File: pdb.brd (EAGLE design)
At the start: 50 x 100 mm, 40 parts, among them Q1 20MHz, Q2 IRFR5305PBF, Q3 IRFR5305PBF, U1 TSR_1-2433, U2 LTC2946CMSPBF, U3 LTC2946CMSPBF, U4 LTC2946CMSPBF, U5 ATMEGA48-20AU, U6 TXB0104, U7 AT30TS74SS8M

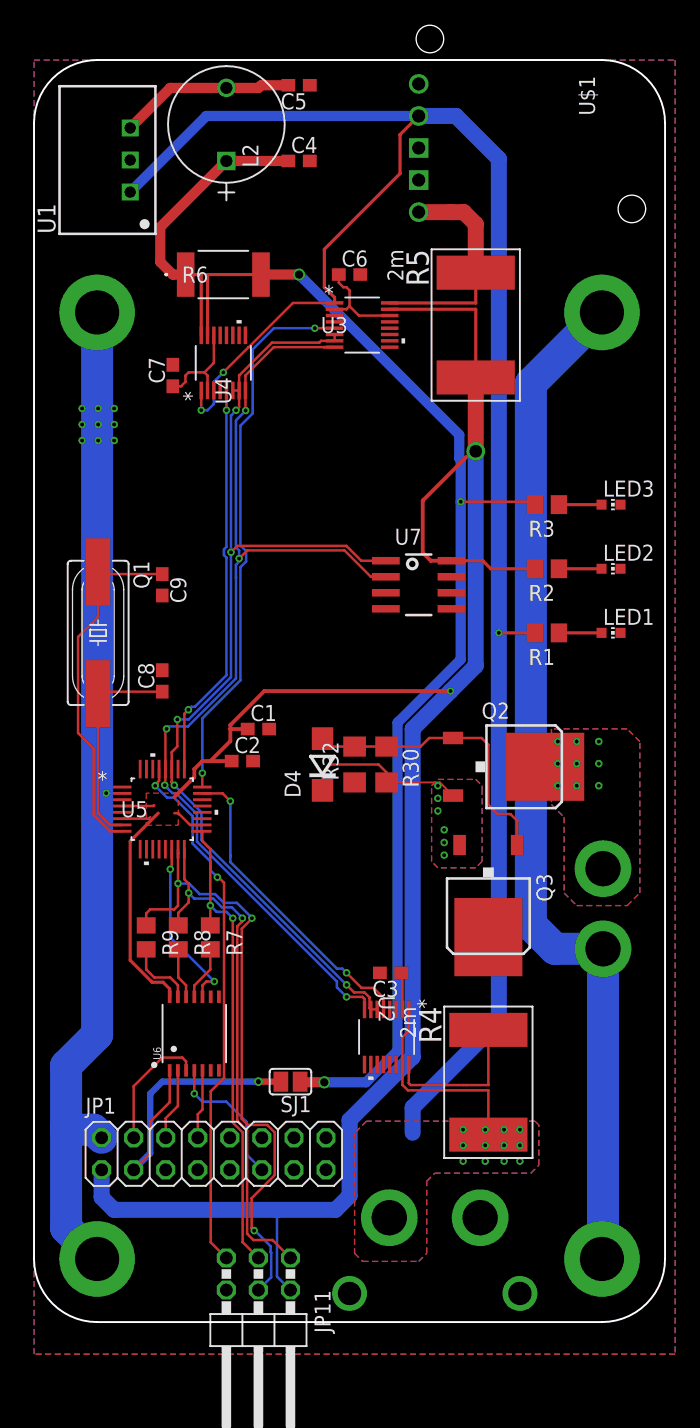
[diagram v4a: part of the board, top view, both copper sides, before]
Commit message: multiple changes
removed inductor,
fixed layout + schematic
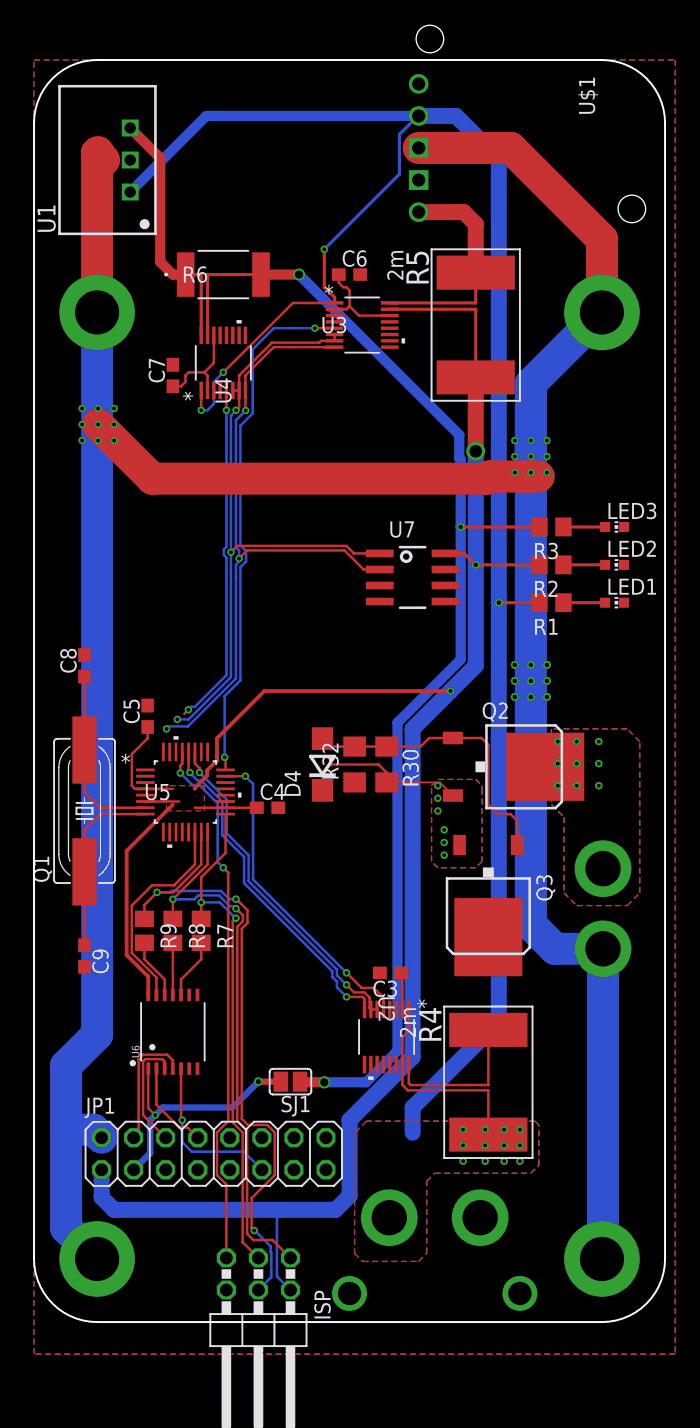
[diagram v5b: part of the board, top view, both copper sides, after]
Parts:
- removed C1, C2: 100nF, rcl:C0603
- removed L2: RLB9012-221KL, jonas_bourns:IND_BOURNS_RLB9012
- C4, C5: device resistor:C0603 -> rcl:C0603
- moved C5 51.4 mm to (9.00, 48.0), turned to 90 degrees
- moved C4 51.3 mm to (18.5, 40.8)
- moved C9 30.1 mm to (4.00, 29.0)
- moved Q1 14.2 mm to (4.00, 40.5), turned to 90 degrees
- moved C8 6.28 mm to (4.00, 52.0)
- moved R1 2.42 mm to (41.0, 57.0)
- moved LED1 2.41 mm to (46.0, 57.0)
- moved U5 2.29 mm to (12.0, 42.0)
- moved R3 1.81 mm to (41.0, 63.0)
- moved LED3 1.79 mm to (46.0, 63.0)
- moved U6 1.71 mm to (11.0, 23.0)
- moved R7 0.89 mm to (13.2, 31.0)
- moved U7 0.75 mm to (30.0, 59.0)
- moved R8 0.67 mm to (11.0, 31.0)
- moved R9 0.54 mm to (8.75, 31.0)
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- renumbered JP11 to ISP
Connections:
- removed net N$6: C5.2, L2.2, U1.3
- removed net N$8: R7.2, U6.11
- new net N$3: R7.2, U6.10
- net +5V: now also C4.1, C5.1; no longer C1.1, C2.1
- net EXT_SPI_CLK: now also U6.5; no longer U6.4
- net EXT_SPI_CS: now also U6.2; no longer U6.5
- net EXT_SPI_MISO: now also U6.4; no longer U6.3
- net EXT_SPI_MOSI: now also U6.3; no longer U6.2
- net GND: now also C5.2; no longer C1.2, C2.2, C5.1
- net N$1: now also R8.2, U6.11; no longer R9.2, U6.13
- net N$2: now also R9.2; no longer R8.2
- net SENSE+3V3: now also U1.3; no longer C4.1, L2.1
- net SS_5V: now also U6.13; no longer U6.10
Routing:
- net GND: track 162.1 -> 240.8 mm, vias 15 -> 32
- net N$6: track 13.9 -> 0.00 mm
- net N$28: track 28.4 -> 14.5 mm
- net +5V: track 183.4 -> 176.7 mm, vias 2 -> 3
- net EXT_3V3: track 26.4 -> 20.0 mm, vias 1 -> 2
- net N$3: track 0.00 -> 4.79 mm
- net !ALERT_3V3: track 31.7 -> 27.3 mm
- net N$8: track 4.28 -> 0.00 mm
- net SDA: track 83.4 -> 79.2 mm
- net EXT_SPI_MOSI: track 5.74 -> 9.35 mm
- net SENSE+3V3: track 23.6 -> 20.1 mm
- net SCL: track 82.2 -> 78.9 mm
- net SS_5V: track 13.9 -> 16.8 mm, vias 2 -> 0
- net MISO_5V: track 41.5 -> 44.3 mm
- net MOSI_5V: track 48.9 -> 51.5 mm
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
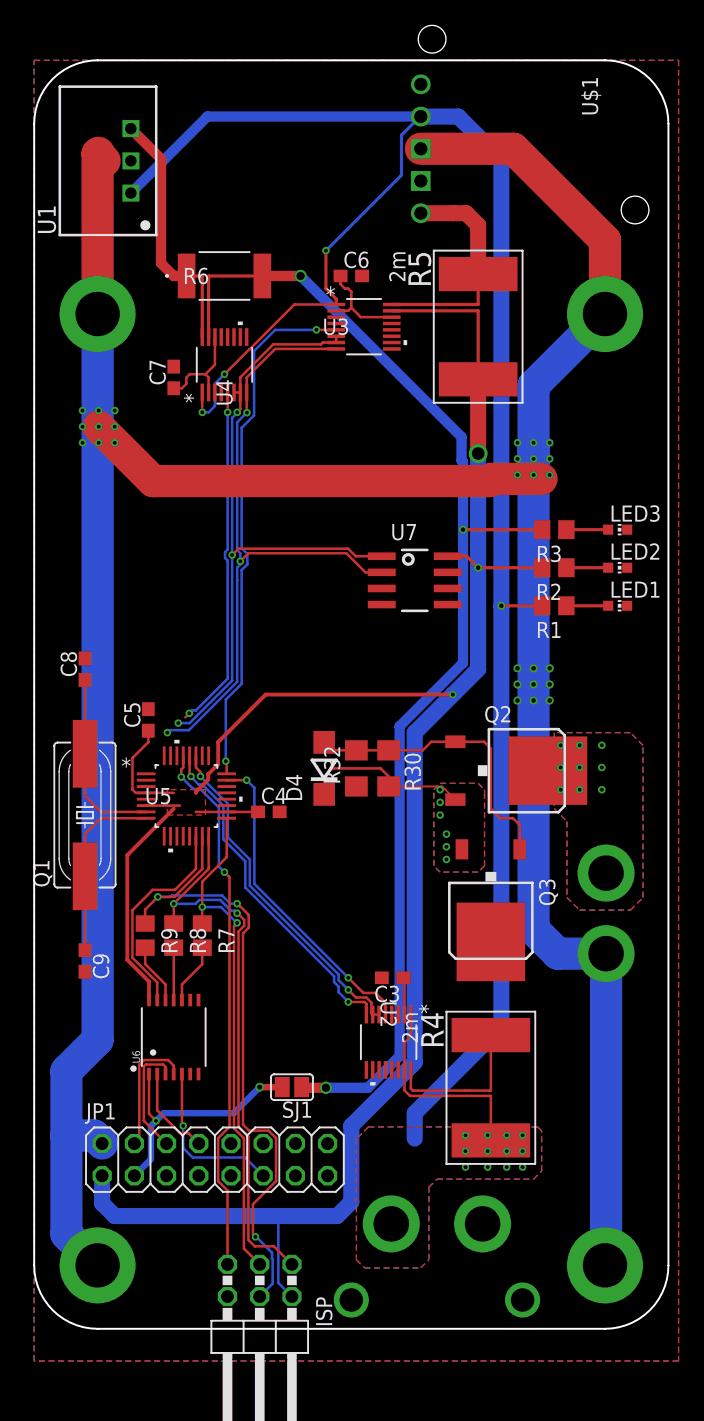
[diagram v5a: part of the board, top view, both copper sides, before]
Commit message: various changes
moved smd components on metric grid
silkscreen, reduced fuckup in part sizes
added output
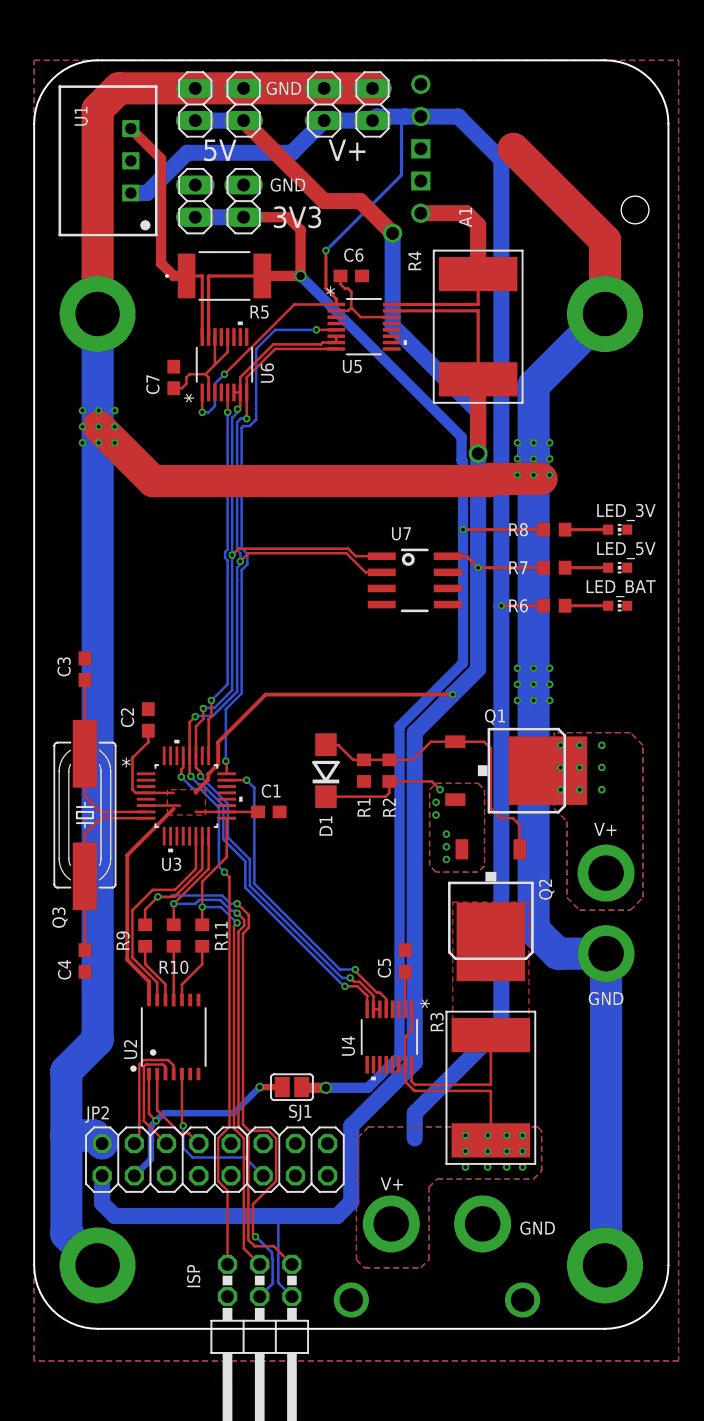
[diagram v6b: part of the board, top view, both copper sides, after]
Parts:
- removed C8, C9: 22pF, rcl:C0603
- removed D4: ZD18, diode:DO214BA
- removed R30: 10k, rcl:R1206
- removed R32: 1k, rcl:R1206
- removed U$1: D24V50F5, niklas_pololu:D24V50F5
- added A1: D24V50F5SINGLESCREW, jonas_pololu:D24V50F5_SINGLESCREW
- added C1, C2: 100nF, resistor:C0603
- added D1: ZD18, diode:DO214BA
- added JP2: (no value), pinhead:2X08
- added JP3, JP4, JP5, JP6, JP7: (no value), pinhead:1X02
- added R10, R11: 4,7k, resistor:R0603
- C3: value 0,1µF -> 22pF; device rcl:C0603 -> resistor:C0603
- C4: value 100nF -> 22pF; device rcl:C0603 -> resistor:C0603
- C5: value 100nF -> 0,1µF; device rcl:C0603 -> resistor:C0603
- C6, C7: device rcl:C0603 -> resistor:C0603
- JP1: device pinhead:2X08 -> pinhead:1X02
- Q1: value 20MHz -> IRFR5305PBF; device crystal:HC49UP -> transistor-power:D-PAK_TO252AA
- Q3: value IRFR5305PBF -> 20MHz; device transistor-power:D-PAK_TO252AA -> crystal:HC49UP
- R1: value 1,2k -> 1k; device rcl:R0805 -> resistor:R0603
- R2: value 250 -> 10k; device rcl:R0805 -> resistor:R0603
- R3: value 100 -> 2m; device rcl:R0805 -> jonas_resistor:3920
- R5: value 2m -> CRA2512-FZ-R040ELF; device jonas_resistor:3920 -> jonas_bourns:BO_CRA2512
- R6: value CRA2512-FZ-R040ELF -> 1,2k; device jonas_bourns:BO_CRA2512 -> resistor:R0603
- R7: value 4,7k -> 250; device rcl:R0805 -> resistor:R0603
- R8: value 4,7k -> 100; device rcl:R0805 -> resistor:R0603
- R9: device rcl:R0805 -> resistor:R0603
- U2: value LTC2946CMSPBF -> TXB0104; device niklas_lt:MSOP-16_MS -> SparkFun-IC-Comms:TSSOP14
- U3: value LTC2946CMSPBF -> ATMEGA48-20AU; device niklas_lt:MSOP-16_MS -> niklas_atmel:32A
- U5: value ATMEGA48-20AU -> LTC2946CMSPBF; device niklas_atmel:32A -> niklas_lt:MSOP-16_MS
- U6: value TXB0104 -> LTC2946CMSPBF; device SparkFun-IC-Comms:TSSOP14 -> niklas_lt:MSOP-16_MS
- moved JP1 84.1 mm to (26.7, 96.5), turned to 90 degrees
- moved R4 60.0 mm to (35.0, 79.0)
- moved U4 54.6 mm to (28.0, 23.0), turned to 270 degrees
- moved U6 53.2 mm to (15.0, 76.0), turned to 90 degrees
- moved R3 44.3 mm to (36.0, 19.0), turned to 270 degrees
- moved R8 43.9 mm to (41.0, 63.0), turned to 180 degrees
- moved R7 40.1 mm to (41.0, 60.0), turned to 180 degrees
- moved U3 39.6 mm to (12.0, 42.0)
- moved U5 39.6 mm to (26.0, 79.0)
- moved R6 36.8 mm to (41.0, 57.0), turned to 180 degrees
- moved C3 34.4 mm to (4.00, 52.0), turned to 90 degrees
- moved Q1 34.2 mm to (38.0, 44.0), turned to 270 degrees
- moved Q3 32.9 mm to (4.00, 40.5), turned to 90 degrees
- moved C5 27.8 mm to (29.2, 29.0)
- moved R2 20.6 mm to (28.0, 44.0), turned to 270 degrees
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- renumbered ESC to J1, LED1 to LED_BAT, LED2 to LED_5V, LED3 to LED_3V
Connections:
- net !ALERT_3V3: now also U3.25, U6.5; no longer U4.5, U5.25
- net !ALERT_5V: now also U3.24, U5.5; no longer U3.5, U5.24
- net !ALERT_V+: now also U3.23, U4.5; no longer U2.5, U5.23
- net +3V3: now also JP6.1, JP7.1, R5.2, R8.2, U6.15; no longer R3.2, R6.2, U4.15
- net +5V: now also C1.1, C2.1, JP2.1, JP4.1, JP5.1, R4.P$2, R7.2, U2.14, U3.18, U3.4, U3.6, U5.15; no longer C4.1, C5.1, JP1.1, R2.2, R5.P$2, U3.15, U5.18, U5.4, U5.6, U6.14
- net AKKU-ZWISCHEN: now also D1.C, Q1.3, R2.2; no longer D4.C, Q3.3, R30.2
- net BAT_IN: now also Q1.4; no longer Q2.4
- net EXT_!RST: now also JP2.16; no longer JP1.16
- net EXT_3V3: now also JP2.3, U2.1; no longer JP1.3, U6.1
- net EXT_A0: now also JP2.9; no longer JP1.9
- net EXT_A3: now also JP2.7; no longer JP1.7
- net EXT_A4: now also JP2.5; no longer JP1.5
- net EXT_D1: now also JP2.14; no longer JP1.14
- net EXT_D2: now also JP2.12; no longer JP1.12
- net EXT_D9: now also JP2.10; no longer JP1.10
- net EXT_SCL_5V: now also JP2.13; no longer JP1.13
- net EXT_SDA_5V: now also JP2.15; no longer JP1.15
- net EXT_SPI_CLK: now also JP2.11, U2.5; no longer JP1.11, U6.5
- net EXT_SPI_CS: now also JP2.8, U2.2; no longer JP1.8, U6.2
- net EXT_SPI_MISO: now also JP2.4, U2.4; no longer JP1.4, U6.4
- net EXT_SPI_MOSI: now also JP2.6, U2.3; no longer JP1.6, U6.3
- net GND: now also A1.3, A1.4, C1.2, C2.2, JP2.2, JP3.2, JP4.2, JP5.2, JP6.2, JP7.2, R1.1, U2.7, U3.21, U3.3, U3.5, U4.12, U4.14, U5.11, U5.12, U6.11; no longer C8.2, C9.2, R32.1, U$1.3, U$1.4, U2.11, U2.12, U2.14, U3.11, U3.12, U5.21, U5.3, U5.5, U6.7
- net GPIO1_3V3: now also U6.3; no longer U4.3
- net GPIO1_5V: now also U5.3; no longer U3.3
- net GPIO1_V+: now also U4.3; no longer U2.3
- net GPIO2_3V3: now also U6.4; no longer U4.4
- net GPIO2_5V: now also U5.4; no longer U3.4
- net GPIO2_V+: now also U4.4; no longer U2.4
- net INTVCC_3V3: now also U6.12, U6.14, U6.2; no longer U4.12, U4.14, U4.2
- net INTVCC_5V: now also U5.14, U5.2; no longer U3.14, U3.2
- net INTVCC_V+: now also C5.1, U4.2; no longer C3.1, U2.2
- net MISO_5V: now also R10.1, U3.16; no longer R8.1, U5.16
- net MOSI_5V: now also U3.15; no longer U5.15
- net N$1: now also R10.2, U2.11; no longer R8.2, U6.11
- net N$2: now also U2.12; no longer U6.12
- net N$27: now also C3.1, Q3.2, U3.7; no longer C8.1, Q1.2, U5.7
- net N$28: now also C4.1, Q3.1, U3.8; no longer C9.1, Q1.1, U5.8
- net N$3: now also R11.2, U2.10; no longer R7.2, U6.10
- net N$4: now also R6.1; no longer R1.1
- net N$41: now also D1.A, Q1.1, R1.2, R2.1; no longer D4.A, Q3.1, R30.1, R32.2
- net N$5: now also R7.1; no longer R2.1
- net N$7: now also R8.1; no longer R3.1
- net RESET: now also U3.29; no longer U5.29
- net SCK_5V: now also R11.1, U3.17; no longer R7.1, U5.17
- net SCL: now also U3.28, U5.8, U6.8; no longer U2.8, U3.8, U5.28
- net SDA: now also U3.27, U5.6, U5.7, U6.6, U6.7; no longer U2.6, U2.7, U3.6, U3.7, U5.27
- net SENSE+3V3: now also R5.1, U6.16; no longer R6.1, U4.16
- net SENSE+5V: now also A1.5, R4.P$1, U5.16; no longer R5.P$1, U$1.5, U3.16
- net SENSE+V+: now also Q2.4, R3.P$1, U4.16; no longer Q3.4, R4.P$1, U2.16
- net SS_5V: now also U2.13, U3.14; no longer U5.14, U6.13
- net V+: now also A1.2, JP1.1, JP3.1, R3.P$2, R6.2, U4.15, U5.1, U6.1; no longer R1.2, R4.P$2, U$1.2, U2.1, U2.15, U3.1
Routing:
- net +5V: track 176.7 -> 216.2 mm, vias 3 -> 4
- net GND: track 240.8 -> 258.4 mm
- net +3V3: track 96.0 -> 108.4 mm
- net AKKU-ZWISCHEN: track 13.5 -> 10.3 mm
- net INTVCC_3V3: track 8.03 -> 10.6 mm
- net !ALERT_3V3: track 27.3 -> 29.4 mm
- net SDA: track 79.2 -> 80.9 mm
- net SENSE+V+: track 12.2 -> 11.6 mm
- net SCL: track 78.9 -> 79.6 mm
- added copper zone on layer 1, net SENSE+V+
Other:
- board text added: "3V3"
- board text added: "5V"
- board text added: "GND"
- board text added: "V+"

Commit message: fixed 3d models
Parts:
- C1, C2, C3, C4, C5, C6, C7: device resistor:C0603 -> rcl:C0603
- R1, R10, R11, R2, R6, R7, R8, R9: device resistor:R0603 -> rcl:R0603

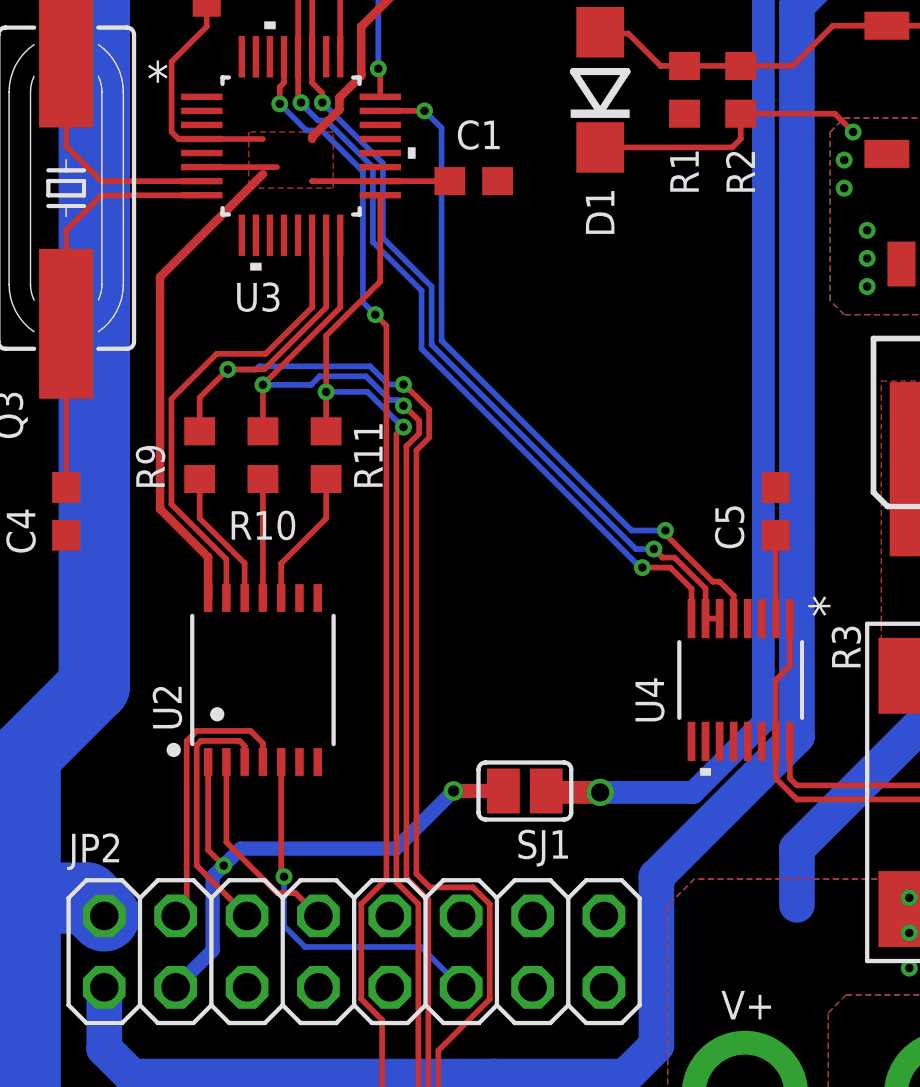
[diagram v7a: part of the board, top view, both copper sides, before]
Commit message: added reset, closed #11
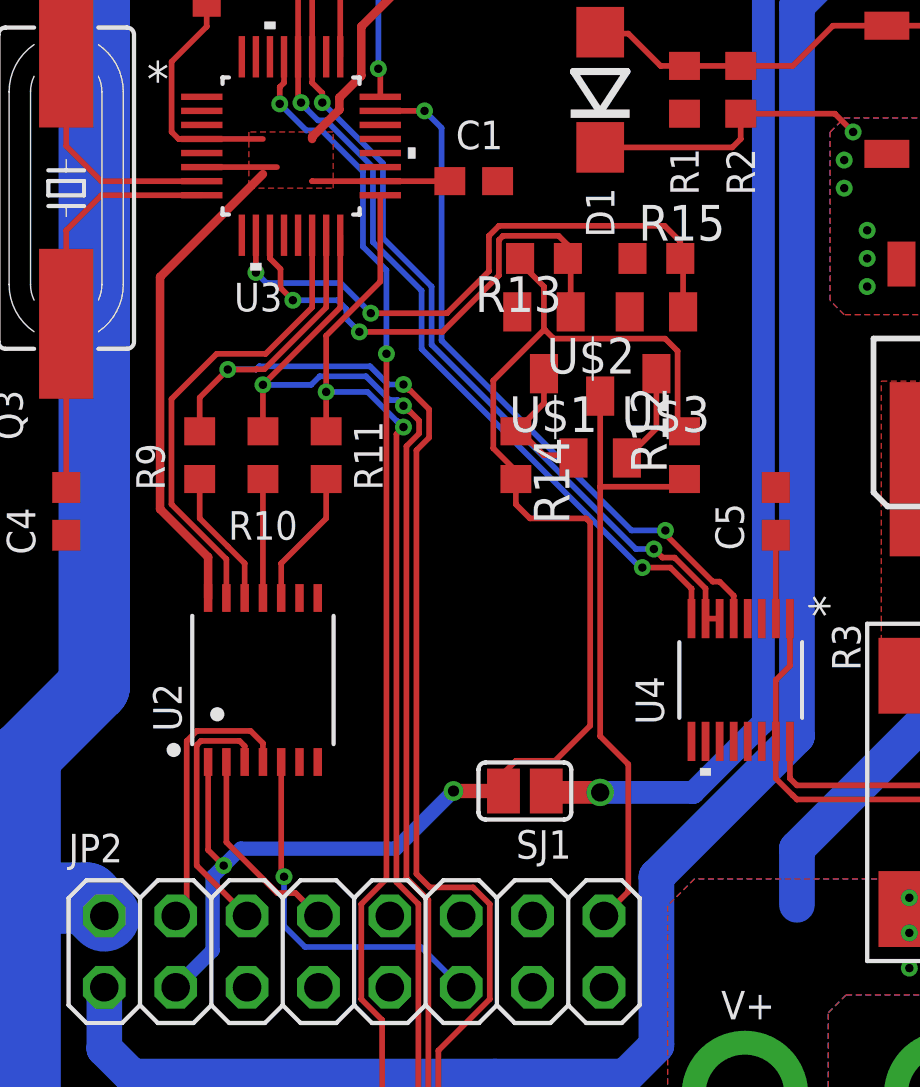
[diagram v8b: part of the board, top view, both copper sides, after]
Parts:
- added R12, R14, R15: 4k7, rcl:R0603
- added R13: 4K7, rcl:R0603
- added U$1, U$2, U$3: BSN20,215, jonas_mosfet:BSN20_215
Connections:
- new net N$11: U$2.2, U$3.3
- new net N$9: R14.1, U$1.3, U$2.1
- new net RST_H: R15.2, U$3.1, U3.10
- new net RST_L: R13.1, U$1.1, U3.11
- net EXT_!RST: now also R12.1, U$2.3
- net EXT_3V3: now also R12.2, R13.2, R14.2
- net GND: now also R15.1, U$1.2, U$3.2
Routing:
- net EXT_3V3: track 20.0 -> 52.8 mm
- net EXT_!RST: track 0.00 -> 22.8 mm
- net RST_H: track 0.00 -> 21.8 mm, vias 0 -> 2
- net RST_L: track 0.00 -> 17.8 mm, vias 0 -> 2
- net N$9: track 0.00 -> 4.86 mm
- net N$11: track 0.00 -> 3.43 mm
